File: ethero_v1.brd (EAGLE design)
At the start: 20 parts, among them IC1 ENC28J60SP, X1 GLX-S-88M

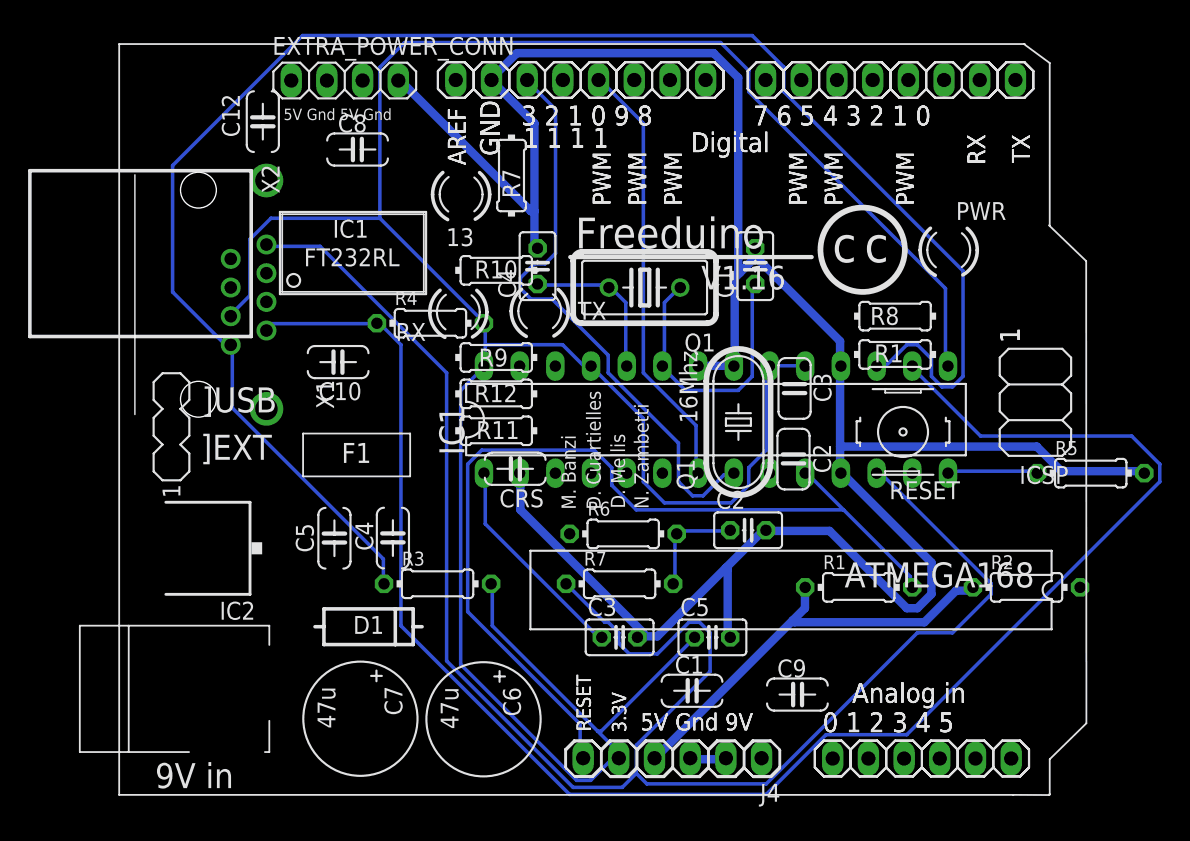
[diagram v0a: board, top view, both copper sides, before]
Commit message: added non inverting buffer for level switching
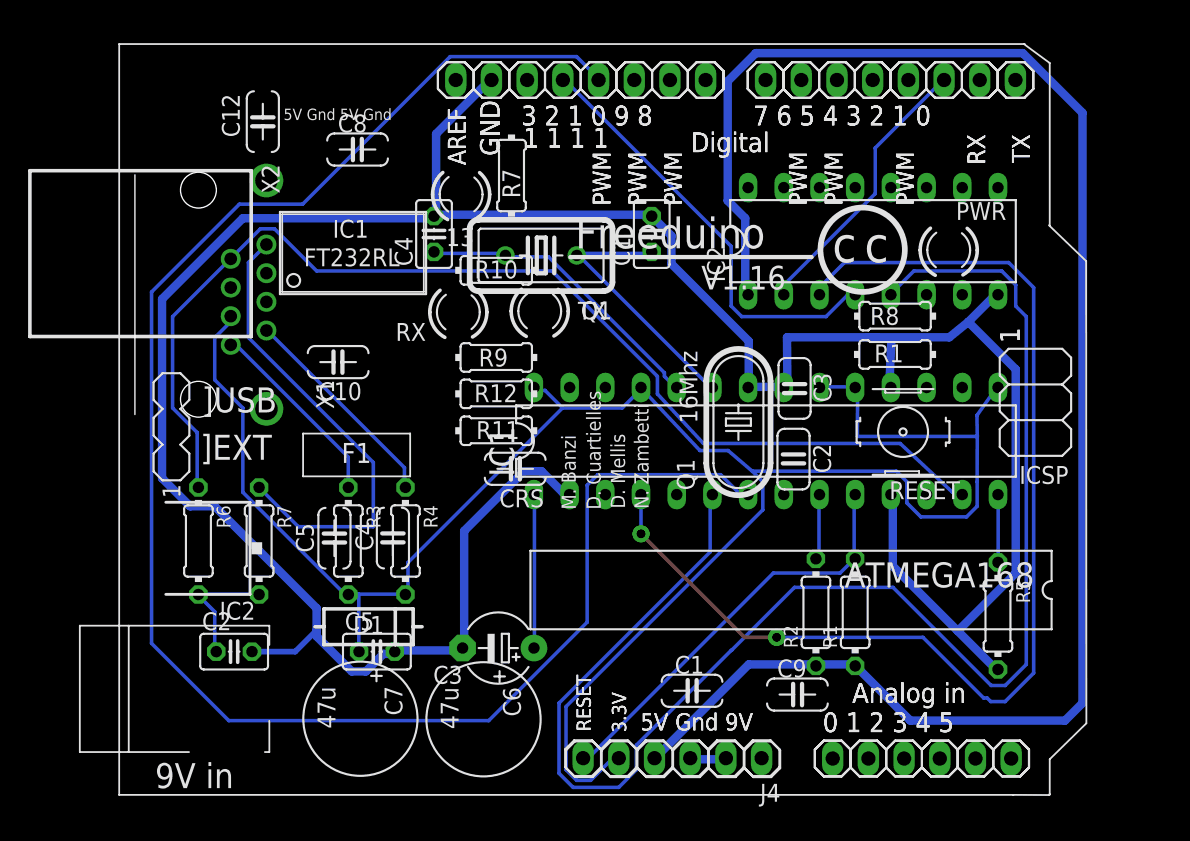
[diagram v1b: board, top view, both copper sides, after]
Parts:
- removed EXTRA_POWER_CONN: (no value), pinhead:1X04
- added IC2: 4050N, 40xx:DIL16
- C3: device resistor:C025-025X050 -> rcl:E5-5
- moved C2 37.6 mm to (8.13, 10.2)
- moved R6 30.2 mm to (5.59, 18.0), turned to 270 degrees
- moved R7 25.8 mm to (9.91, 18.0), turned to 270 degrees
- moved C5 23.9 mm to (18.3, 10.2)
- moved R4 15.6 mm to (20.3, 18.0), turned to 270 degrees
- moved R2 15.1 mm to (49.5, 13.0), turned to 90 degrees
- moved R5 12.1 mm to (62.5, 12.7), turned to 270 degrees
- moved C3 8.67 mm to (26.9, 10.4), turned to 180 degrees
- moved C1 7.71 mm to (37.8, 39.9)
- moved C4 7.71 mm to (22.4, 39.9)
- moved Q1 7.71 mm to (30.0, 38.4)
- moved R3 7.04 mm to (16.3, 18.0), turned to 270 degrees
- moved IC1 3.87 mm to (46.0, 25.1)
- moved R1 1.80 mm to (52.3, 13.0), turned to 90 degrees
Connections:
- removed net V5.0: EXTRA_POWER_CONN.1
- new net INT: IC1.4, IC2.3
- new net SO: IC1.6, IC2.5
- net DCV: now also IC2.1; no longer EXTRA_POWER_CONN.3
- net GND: now also C3.-, IC2.8; no longer C3.2, EXTRA_POWER_CONN.2, EXTRA_POWER_CONN.4
- net INT0: now also IC2.2
- net MISO: now also IC2.4
- net VCAP: now also C3.+; no longer C3.1
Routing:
- net TPOUTP: track 121.1 -> 13.9 mm
- net SO: track 0.00 -> 105.8 mm
- net TPOUTM: track 120.5 -> 15.3 mm
- net MOSI/OC2: track 31.0 -> 122.8 mm
- net DCV: track 30.5 -> 121.1 mm
- net TPINM: track 124.4 -> 33.9 mm
- net INT: track 0.00 -> 81.2 mm, vias 0 -> 2
- net TPINP: track 0.00 -> 80.3 mm
- net V3.3: track 196.7 -> 144.6 mm
- net SCK: track 41.4 -> 0.00 mm
- net RESET: track 65.4 -> 29.9 mm
- net MISO: track 0.00 -> 30.9 mm
- net GND: track 170.7 -> 199.4 mm
- net INT0: track 0.00 -> 20.0 mm
- net OSC2: track 11.5 -> 21.4 mm
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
